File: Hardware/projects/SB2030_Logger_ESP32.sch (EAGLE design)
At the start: 20 parts, among them SW1 CKTACTSWITCH, U1 ESP-WROOM-32, U2 MCP2562, U3 NCP1117ST50T3G, U4 NCP1117ST33T3G

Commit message: Updates to hardware prototype design to support RS422 input, and added separate RS422 for Arduino Due for testing purposes.
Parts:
- added C11, C12, C13: 0.1u, rcl:C-EUC0805
- added D1, D2: 1N5819, sb2030_logger:1N5819HW-7-F
- added OK1, OK2: H11L1MS, optocoupler:H11L1MS
- added R3, R4: 1k2, rcl:R-EU_R0805
- added R5, R6: 10k, rcl:R-EU_R0805
- added U5: SN65C1168PWR, sb2030_logger:SN65C1168PWR
- added U6: (no value), sb2030_logger:RFM-0505S
- added X1: 1751280, con-phoenix-350:1751280
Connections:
- removed net N$11: C1.2
- new net +12V: D1.1, X1-2.K
- new net GNDI: C11.2, U5.1D, U5.1DE, U5.2D, U5.2DE, U5.GND, U6.V-OUT
- new net N$13: OK1.C, U5.1R
- new net N$14: OK2.C, U5.2R
- new net N$15: OK1.A, R4.1
- new net N$16: OK2.A, R3.1
- new net N$17: U5.1A, X1-6.K
- new net N$18: U5.1B, X1-5.K
- new net N$19: U5.2A, X1-4.K
- new net N$20: U5.2B, X1-3.K
- new net N$21: C11.1, R3.2, R4.2, U5.VCC, U6.V+OUT
- new net N$22: D2.1, JP2.12V
- new net RX1: OK1.OUT, R5.1, U1.IO12
- new net RX2: OK2.OUT, R6.1, U1.IO14
- net +3V3: now also C12.1, C13.1, OK1.VCC, OK2.VCC, R5.2, R6.2
- net +5V: now also U6.V+IN
- net GND: now also C1.2, C12.2, C13.2, JP2.GND, OK1.GND, OK2.GND, U6.V-IN, X1-1.K; no longer JP2.3
- net N$1: now also JP2.CAN-H; no longer JP2.4
- net N$2: now also JP2.CAN-L; no longer JP2.5
- net VIN: now also D1.2, D2.2; no longer JP2.2

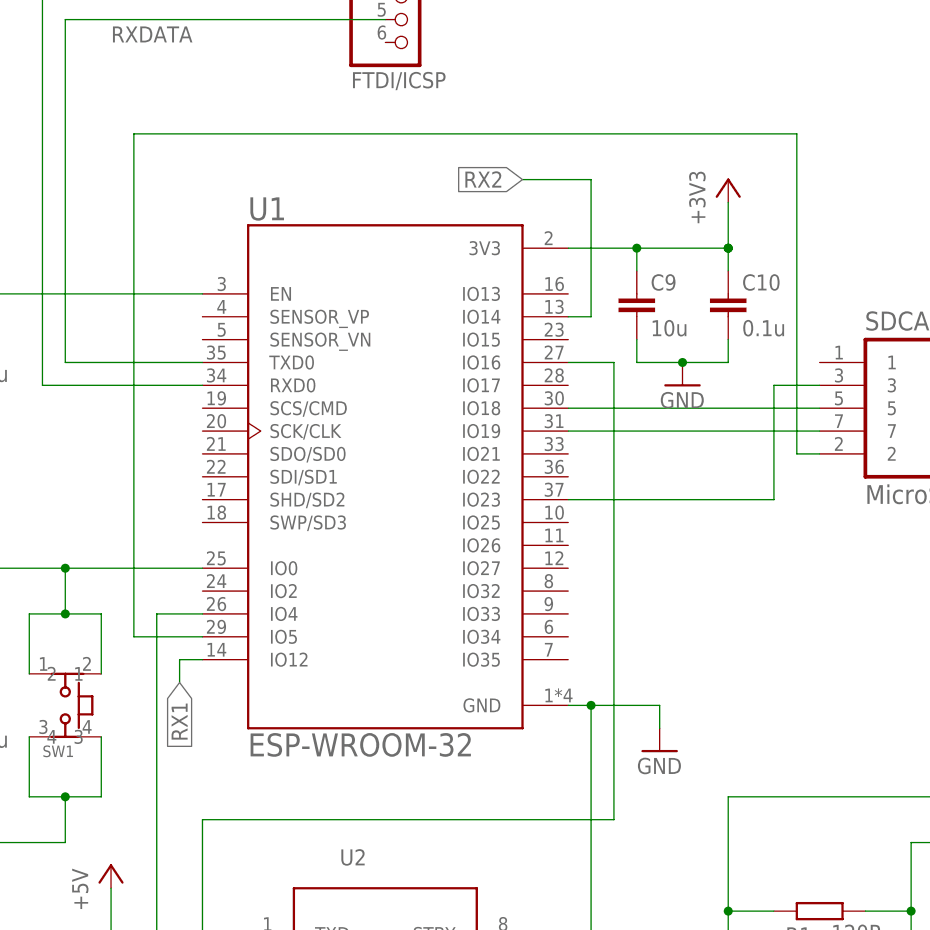
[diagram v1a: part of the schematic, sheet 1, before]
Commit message: Update to ESP32-based hardware to accommodate NMEA0183 input pins that don't cause boot problems (GPIO12 is used to set Flash voltage on boot, so having an active data stream attached causes all sorts of problems at boot time).
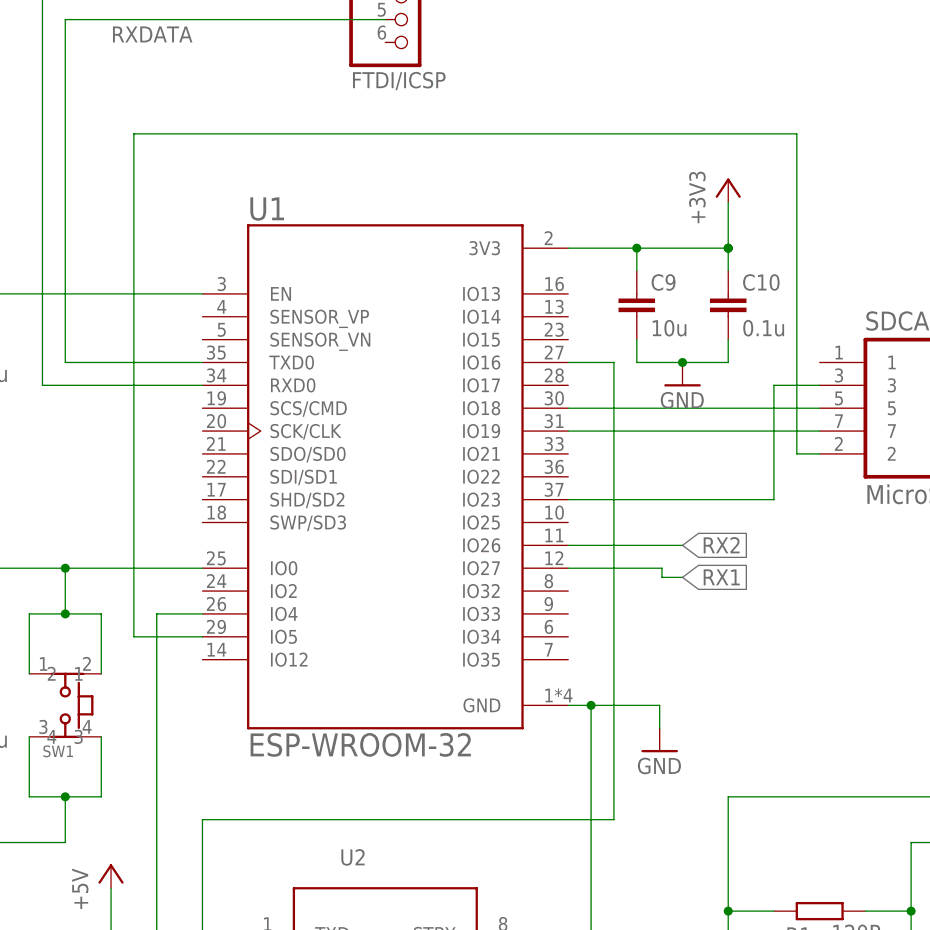
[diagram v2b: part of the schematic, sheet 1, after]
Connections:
- net RX1: now also U1.IO27; no longer U1.IO12
- net RX2: now also U1.IO26; no longer U1.IO14
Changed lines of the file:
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@@
-</segment>
-</net>
-<net name="RX1" class="0">
-<segment>
-<wire x1="43.18" y1="76.2" x2="43.18" y2="73.66" width="0.1524" layer="91"/>
-<label x="43.18" y="73.66" size="1.778" layer="95" rot="R270" xref="yes"/>
-<pinref part="U1" gate="G$1" pin="IO12"/>
-<wire x1="45.72" y1="76.2" x2="43.18" y2="76.2" width="0.1524" layer="91"/>
 </segment>
 </net>
 <net name="RX2" class="0">
 <segment>
-<pinref part="U1" gate="G$1" pin="IO14"/>
-<wire x1="86.36" y1="114.3" x2="88.9" y2="114.3" width="0.1524" layer="91"/>
-<label x="81.28" y="129.54" size="1.778" layer="95" rot="R180" xref="yes"/>
-<wire x1="88.9" y1="114.3" x2="88.9" y2="129.54" width="0.1524" layer="91"/>
-<wire x1="88.9" y1="129.54" x2="81.28" y2="129.54" width="0.1524" layer="91"/>
+<label x="99.06" y="88.9" size="1.778" layer="95" xref="yes"/>
+<pinref part="U1" gate="G$1" pin="IO26"/>
+<wire x1="86.36" y1="88.9" x2="99.06" y2="88.9" width="0.1524" layer="91"/>
 </segment>
 </net>
@@
 </segment>
 </net>
+<net name="RX1" class="0">
+<segment>
+<pinref part="U1" gate="G$1" pin="IO27"/>
+<wire x1="86.36" y1="86.36" x2="96.774" y2="86.36" width="0.1524" layer="91"/>
+<wire x1="96.774" y1="86.36" x2="96.774" y2="85.344" width="0.1524" layer="91"/>
+<wire x1="96.774" y1="85.344" x2="99.06" y2="85.344" width="0.1524" layer="91"/>
+<label x="99.06" y="85.344" size="1.778" layer="95" xref="yes"/>
+</segment>
+</net>

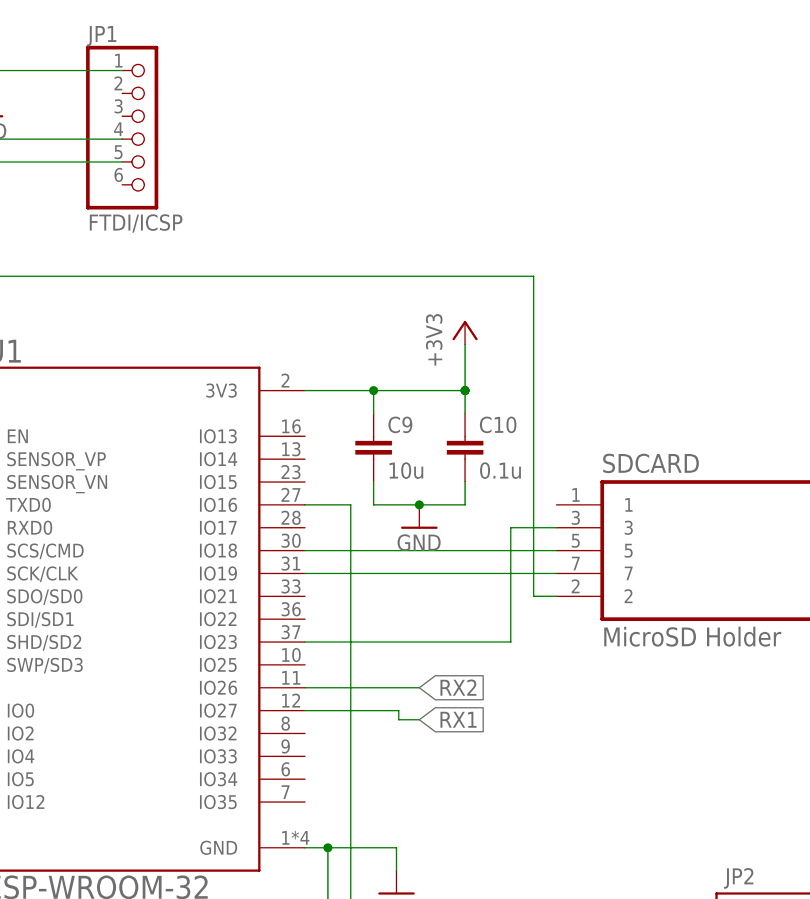
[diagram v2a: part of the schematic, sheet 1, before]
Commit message: Updated schematic for ESP32, and source code, to reflect new choice of UART receiver pins.
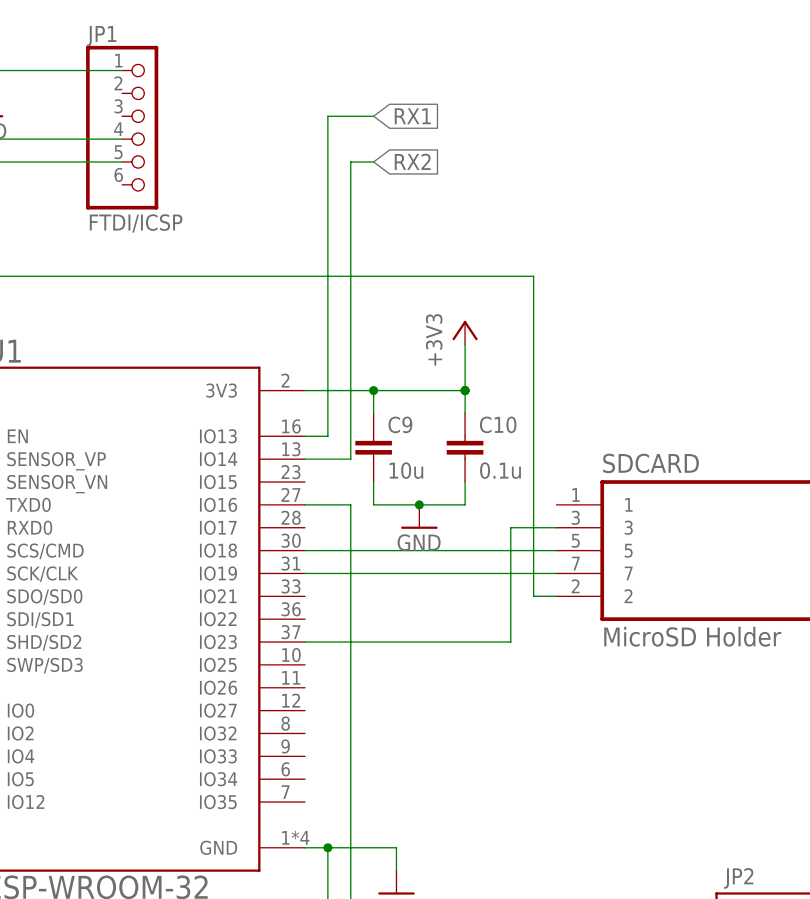
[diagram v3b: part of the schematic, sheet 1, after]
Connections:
- net RX1: now also U1.IO13; no longer U1.IO27
- net RX2: now also U1.IO14; no longer U1.IO26
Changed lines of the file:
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@@
-</segment>
-</net>
-<net name="RX2" class="0">
-<segment>
-<label x="99.06" y="88.9" size="1.778" layer="95" xref="yes"/>
-<pinref part="U1" gate="G$1" pin="IO26"/>
-<wire x1="86.36" y1="88.9" x2="99.06" y2="88.9" width="0.1524" layer="91"/>
 </segment>
 </net>
@@
 <net name="RX1" class="0">
 <segment>
-<pinref part="U1" gate="G$1" pin="IO27"/>
-<wire x1="86.36" y1="86.36" x2="96.774" y2="86.36" width="0.1524" layer="91"/>
-<wire x1="96.774" y1="86.36" x2="96.774" y2="85.344" width="0.1524" layer="91"/>
-<wire x1="96.774" y1="85.344" x2="99.06" y2="85.344" width="0.1524" layer="91"/>
-<label x="99.06" y="85.344" size="1.778" layer="95" xref="yes"/>
+<pinref part="U1" gate="G$1" pin="IO13"/>
+<wire x1="86.36" y1="116.84" x2="88.9" y2="116.84" width="0.1524" layer="91"/>
+<wire x1="88.9" y1="116.84" x2="88.9" y2="152.4" width="0.1524" layer="91"/>
+<wire x1="88.9" y1="152.4" x2="93.98" y2="152.4" width="0.1524" layer="91"/>
+<label x="93.98" y="152.4" size="1.778" layer="95" xref="yes"/>
 </segment>
 </net>
+<net name="RX2" class="0">
+<segment>
+<pinref part="U1" gate="G$1" pin="IO14"/>
+<wire x1="86.36" y1="114.3" x2="91.44" y2="114.3" width="0.1524" layer="91"/>
+<wire x1="91.44" y1="114.3" x2="91.44" y2="147.32" width="0.1524" layer="91"/>
+<wire x1="91.44" y1="147.32" x2="93.98" y2="147.32" width="0.1524" layer="91"/>
+<label x="93.98" y="147.32" size="1.778" layer="95" xref="yes"/>
+</segment>
+</net>
